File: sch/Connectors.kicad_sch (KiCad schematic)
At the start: 4 parts, among them J1 Conn_01x16_Pin, J2 Conn_01x12_Pin, J4 Conn_01x02_MountingPin, J5 Conn_01x04_MountingPin

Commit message: Renamed to RoyalBlue54L-Feather
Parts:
- J1: footprint RoyalBlue-nRF54L15-Connector_PinHeader_2.54mm:PinHeader_1x16_P2.54mm_Vertical -> RoyalBlue54L-Feather-Connector_PinHeader_2.54mm:PinHeader_1x16_P2.54mm_Vertical
- J2: footprint RoyalBlue-nRF54L15-Connector_PinHeader_2.54mm:PinHeader_1x12_P2.54mm_Vertical -> RoyalBlue54L-Feather-Connector_PinHeader_2.54mm:PinHeader_1x12_P2.54mm_Vertical
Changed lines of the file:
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@@
 		)
 		(instances
-			(project "RoyalBlue-nRF54L15"
+			(project "RoyalBlue54L-Feather"
 				(path "/ba76ff89-c129-45ae-a3c9-97538370856c/0a43c989-a862-4ff1-8fb5-5f7c93f777a1"
 					(reference "#PWR06")
@@
 		)
 		(instances
-			(project "RoyalBlue-nRF54L15"
+			(project "RoyalBlue54L-Feather"
 				(path "/ba76ff89-c129-45ae-a3c9-97538370856c/0a43c989-a862-4ff1-8fb5-5f7c93f777a1"
 					(reference "#PWR05")
@@
 		)
 		(instances
-			(project "RoyalBlue-nRF54L15"
+			(project "RoyalBlue54L-Feather"
 				(path "/ba76ff89-c129-45ae-a3c9-97538370856c/0a43c989-a862-4ff1-8fb5-5f7c93f777a1"
 					(reference "#PWR02")
@@
 		)
 		(instances
-			(project "RoyalBlue-nRF54L15"
+			(project "RoyalBlue54L-Feather"
 				(path "/ba76ff89-c129-45ae-a3c9-97538370856c/0a43c989-a862-4ff1-8fb5-5f7c93f777a1"
 					(reference "#PWR04")
@@
 		)
 		(instances
-			(project "RoyalBlue-nRF54L15"
+			(project "RoyalBlue54L-Feather"
 				(path "/ba76ff89-c129-45ae-a3c9-97538370856c/0a43c989-a862-4ff1-8fb5-5f7c93f777a1"
 					(reference "#PWR048")
@@
 		)
 		(instances
-			(project "RoyalBlue-nRF54L15"
+			(project "RoyalBlue54L-Feather"
 				(path "/ba76ff89-c129-45ae-a3c9-97538370856c/0a43c989-a862-4ff1-8fb5-5f7c93f777a1"
 					(reference "J5")
@@
 		)
 		(instances
-			(project "RoyalBlue-nRF54L15"
+			(project "RoyalBlue54L-Feather"
 				(path "/ba76ff89-c129-45ae-a3c9-97538370856c/0a43c989-a862-4ff1-8fb5-5f7c93f777a1"
 					(reference "#PWR09")
@@
 		)
 		(instances
-			(project "RoyalBlue-nRF54L15"
+			(project "RoyalBlue54L-Feather"
 				(path "/ba76ff89-c129-45ae-a3c9-97538370856c/0a43c989-a862-4ff1-8fb5-5f7c93f777a1"
 					(reference "#PWR01")
@@
 		)
 		(instances
-			(project "RoyalBlue-nRF54L15"
+			(project "RoyalBlue54L-Feather"
 				(path "/ba76ff89-c129-45ae-a3c9-97538370856c/0a43c989-a862-4ff1-8fb5-5f7c93f777a1"
 					(reference "#PWR08")
@@
 			)
 		)
-		(property "Footprint" "RoyalBlue-nRF54L15-Connector_PinHeader_2.54mm:PinHeader_1x12_P2.54mm_Vertical"
+		(property "Footprint" "RoyalBlue54L-Feather-Connector_PinHeader_2.54mm:PinHeader_1x12_P2.54mm_Vertical"
 			(at 115.57 101.6 0)
 			(effects
@@
 		)
 		(instances
-			(project "RoyalBlue-nRF54L15"
+			(project "RoyalBlue54L-Feather"
 				(path "/ba76ff89-c129-45ae-a3c9-97538370856c/0a43c989-a862-4ff1-8fb5-5f7c93f777a1"
 					(reference "J2")
@@
 			)
 		)
-		(property "Footprint" "RoyalBlue-nRF54L15-Connector_PinHeader_2.54mm:PinHeader_1x16_P2.54mm_Vertical"
+		(property "Footprint" "RoyalBlue54L-Feather-Connector_PinHeader_2.54mm:PinHeader_1x16_P2.54mm_Vertical"
 			(at 63.5 106.68 0)
 			(effects
@@
 		)
 		(instances
-			(project "RoyalBlue-nRF54L15"
+			(project "RoyalBlue54L-Feather"
 				(path "/ba76ff89-c129-45ae-a3c9-97538370856c/0a43c989-a862-4ff1-8fb5-5f7c93f777a1"
 					(reference "J1")
@@
 		)
 		(instances
-			(project "RoyalBlue-nRF54L15"
+			(project "RoyalBlue54L-Feather"
 				(path "/ba76ff89-c129-45ae-a3c9-97538370856c/0a43c989-a862-4ff1-8fb5-5f7c93f777a1"
 					(reference "#PWR07")
@@
 		)
 		(instances
-			(project "RoyalBlue-nRF54L15"
+			(project "RoyalBlue54L-Feather"
 				(path "/ba76ff89-c129-45ae-a3c9-97538370856c/0a43c989-a862-4ff1-8fb5-5f7c93f777a1"
 					(reference "J4")

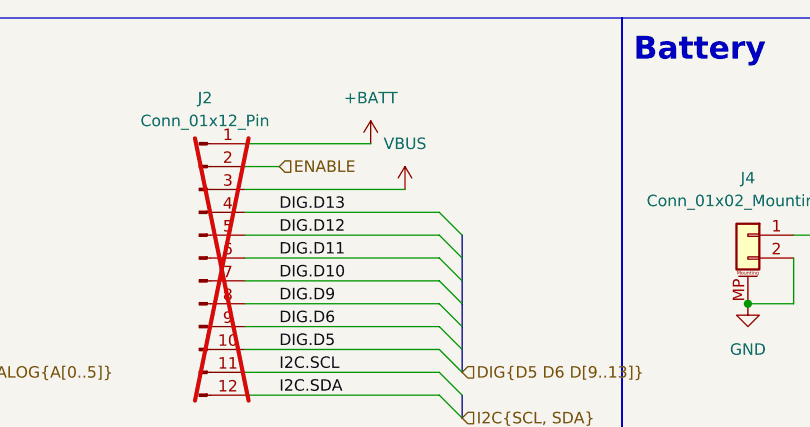
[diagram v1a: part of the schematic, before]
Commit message: Added testpoints, moved USB connection to VSYS.
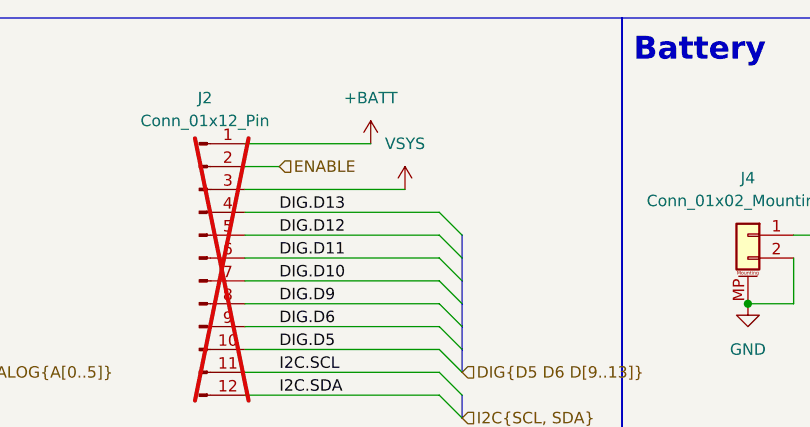
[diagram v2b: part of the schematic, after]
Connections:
- net VBUS renamed VSYS
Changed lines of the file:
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@@
 			)
 		)
-		(property "Value" "VBUS"
+		(property "Value" "VSYS"
 			(at 138.43 88.9 0)
 			(effects
